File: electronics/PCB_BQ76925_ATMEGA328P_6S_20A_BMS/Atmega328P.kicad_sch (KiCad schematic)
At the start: 14 parts, among them J5 Conn_01x04, J6 Conn_02x03_Counter_Clockwise, U2 ATmega328P-A, U3 AMS1117-5.0, Y1 16Mhz

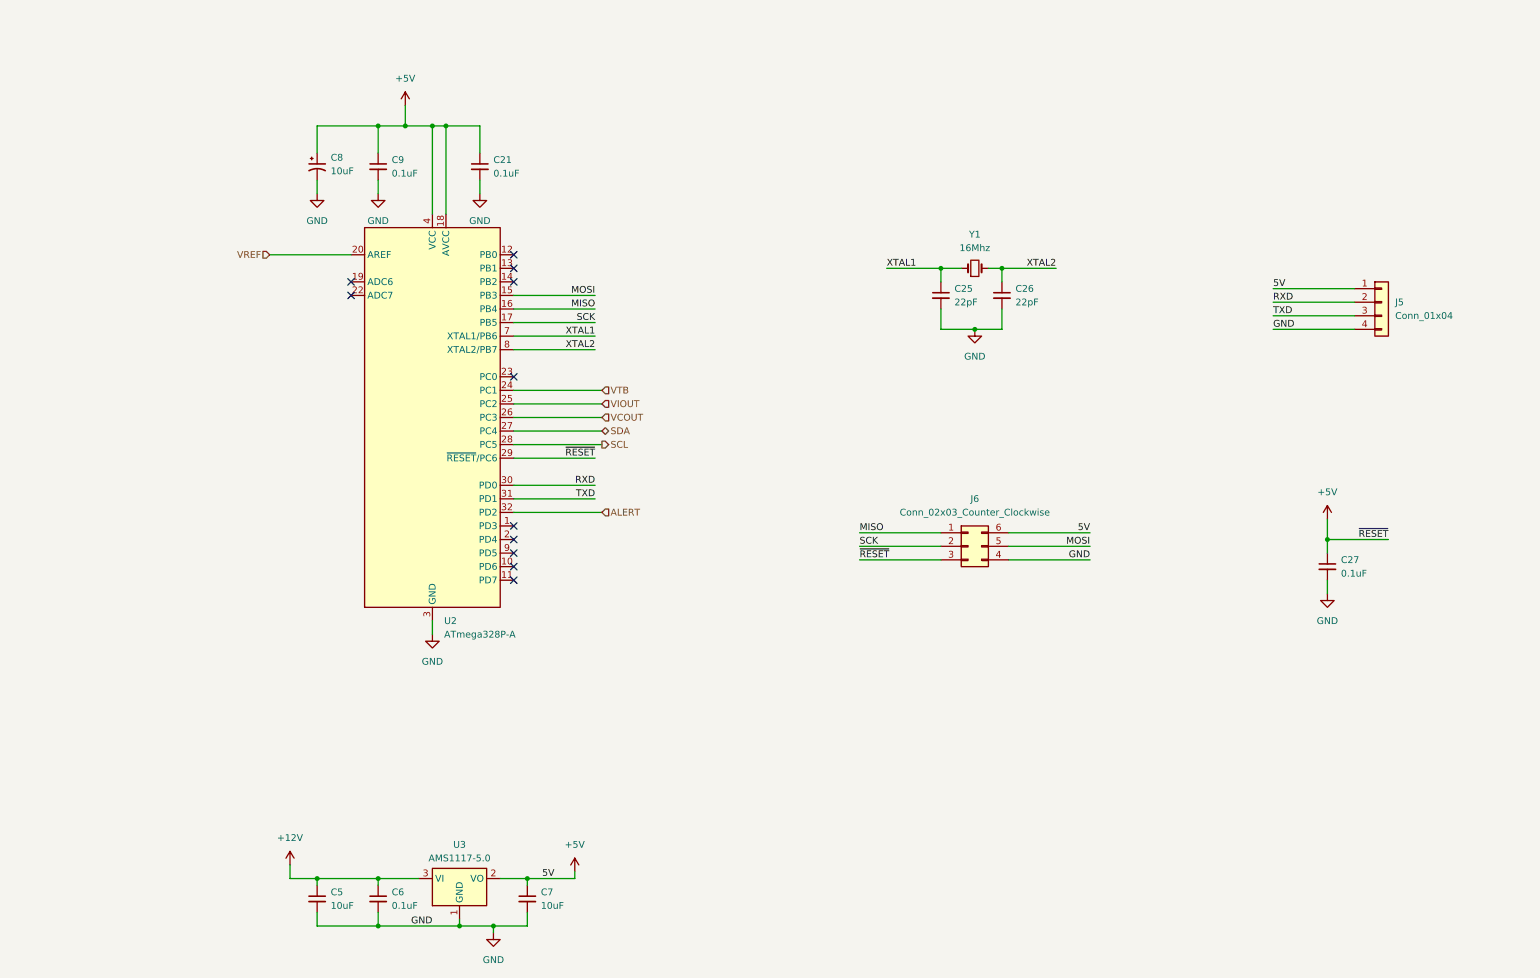
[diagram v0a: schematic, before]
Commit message: schematic completed component need to be finalised
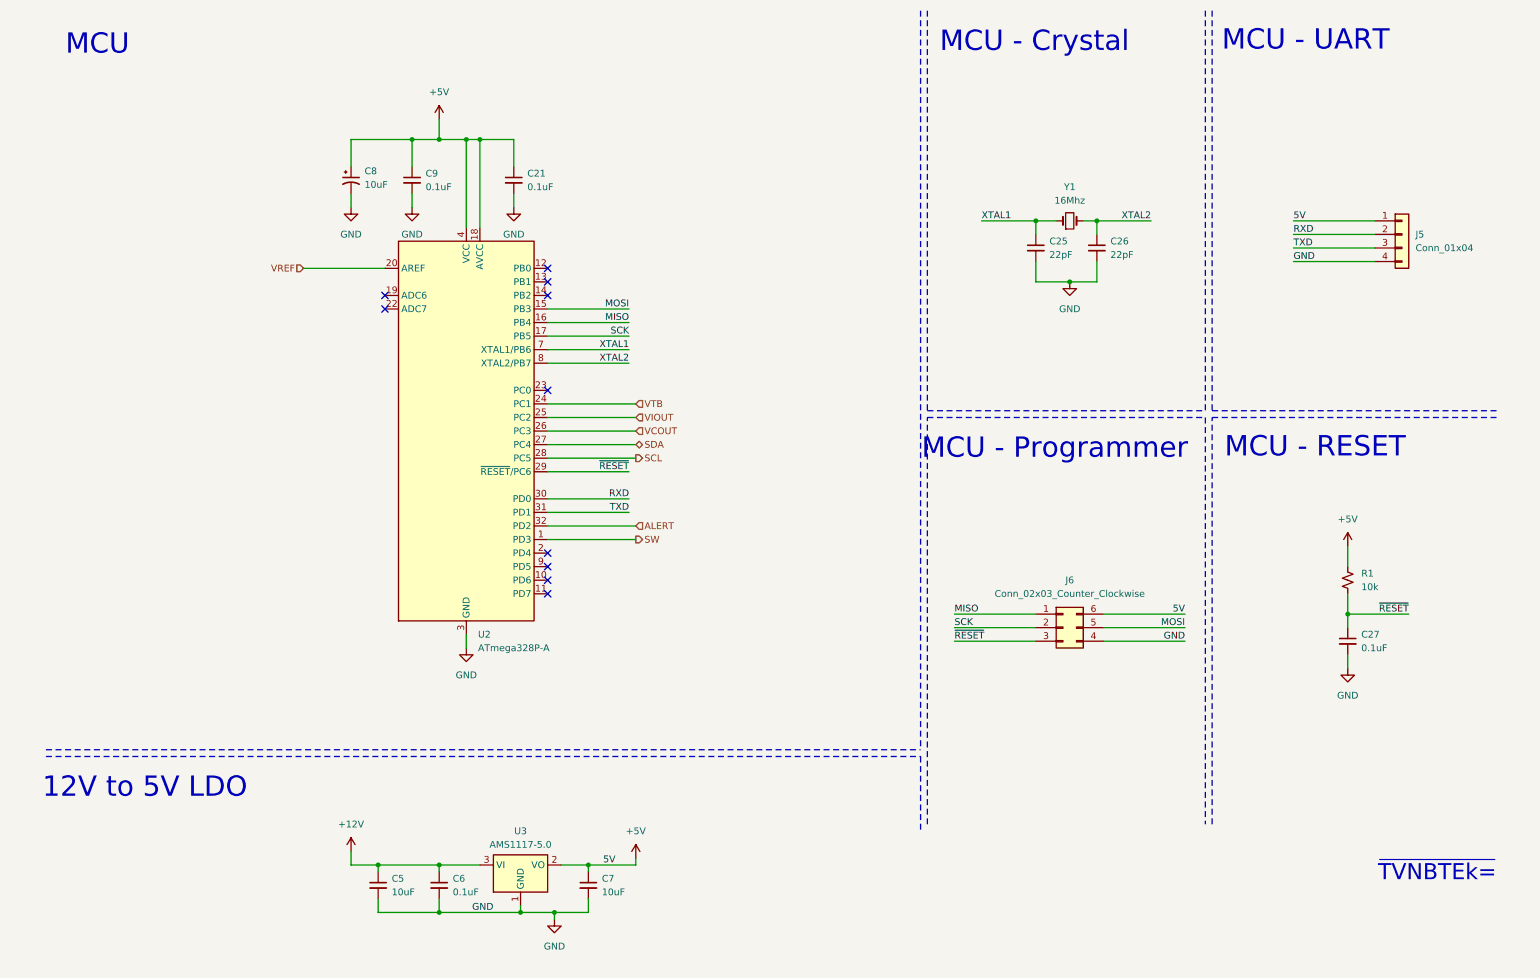
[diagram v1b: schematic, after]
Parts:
- added R1: 10k, symbol BQ76925_ATMEGA328P_6S_20A_BMS:R_Small_US
- J5: symbol Connector_Generic:Conn_01x04 -> BQ76925_ATMEGA328P_6S_20A_BMS:Conn_01x04
- J6: symbol Connector_Generic:Conn_02x03_Counter_Clockwise -> BQ76925_ATMEGA328P_6S_20A_BMS:Conn_02x03_Counter_Clockwise
- Y1: symbol Device:Crystal_Small -> BQ76925_ATMEGA328P_6S_20A_BMS:Crystal_Small
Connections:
- net +5V: now also R1.2; no longer C27.1, J6.3 (Pin_3), U2.29 (~{RESET}/PC6)
- net SW: now reaches U2.1 (PD3)
- new net ~{RESET}: C27.1, J6.3 (Pin_3), R1.1, U2.29 (~{RESET}/PC6)
- no-connect marks 11 -> 10
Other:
- note added: "12V to 5V LDO"
- note added: "MCU"
- note added: "MCU - Crystal"
- note added: "MCU - Programmer"
- note added: "MCU - RESET"
- note added: "MCU - UART"
- note added: "~{TVNBTEk=}"
- company: (none) -> M S Ali
- title: (none) -> Raven-I Sentinel
- moved on the sheet: C21, C25, C26, C27, C5, C6, C7, C8, C9, J5, J6, U2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

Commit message: Schematic completed components calculated need to check avaialability
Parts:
- C21: renamed from C9; footprint (none) -> Capacitor_SMD:C_0603_1608Metric_Pad1.08x0.95mm_HandSolder
- C22: renamed from C21; footprint (none) -> Capacitor_SMD:C_0603_1608Metric_Pad1.08x0.95mm_HandSolder
- C25: renamed from C27; footprint (none) -> Capacitor_SMD:C_0603_1608Metric_Pad1.08x0.95mm_HandSolder
- C27: renamed from C6; footprint (none) -> Capacitor_SMD:C_0603_1608Metric_Pad1.08x0.95mm_HandSolder
- J6: value Conn_02x03_Counter_Clockwise -> Conn_02x03
- R26: renamed from R1; footprint (none) -> Resistor_SMD:R_0603_1608Metric_Pad0.98x0.95mm_HandSolder
- renumbered C8 to C20, C25 to C23, C26 to C24, C5 to C26, C7 to C28, U2 to U3, U3 to U4
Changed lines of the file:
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@@
 	(title_block
 		(title "Raven-I Sentinel")
+		(date "2024-11-23")
 		(company "M S Ali")
 	)
@@
 		(dnp no)
 		(fields_autoplaced yes)
-		(property "Reference" "#PWR01"
+		(property "Reference" "#PWR032"
 			(at 91.44 138.43 0)
 			(effects
@@
 			(project "BQ76925_ATMEGA328P_6S_20A_BMS"
 				(path "/624a087f-322b-4a70-8c29-0e4f8f018e16/e88de734-726e-4991-811a-b88126c63525"
-					(reference "#PWR01")
+					(reference "#PWR032")
 					(unit 1)
 				)
@@
 		(dnp no)
 		(fields_autoplaced yes)
-		(property "Reference" "C27"
+		(property "Reference" "C25"
 			(at 259.08 129.5462 0)
 			(effects
@@
 			)
 		)
-		(property "Footprint" ""
+		(property "Footprint" "Capacitor_SMD:C_0603_1608Metric_Pad1.08x0.95mm_HandSolder"
 			(at 256.54 130.81 0)
 			(effects
@@
 			(project "BQ76925_ATMEGA328P_6S_20A_BMS"
 				(path "/624a087f-322b-4a70-8c29-0e4f8f018e16/e88de734-726e-4991-811a-b88126c63525"
-					(reference "C27")
+					(reference "C25")
 					(unit 1)
 				)
@@
 		(dnp no)
 		(fields_autoplaced yes)
-		(property "Reference" "#PWR029"
+		(property "Reference" "#PWR033"
 			(at 256.54 142.24 0)
 			(effects
@@
 			(project "BQ76925_ATMEGA328P_6S_20A_BMS"
 				(path "/624a087f-322b-4a70-8c29-0e4f8f018e16/e88de734-726e-4991-811a-b88126c63525"
-					(reference "#PWR029")
+					(reference "#PWR033")
 					(unit 1)
 				)
@@
 		(dnp no)
 		(fields_autoplaced yes)
-		(property "Reference" "C25"
+		(property "Reference" "C23"
 			(at 200.66 55.8862 0)
 			(effects
@@
 			(project "BQ76925_ATMEGA328P_6S_20A_BMS"
 				(path "/624a087f-322b-4a70-8c29-0e4f8f018e16/e88de734-726e-4991-811a-b88126c63525"
-					(reference "C25")
+					(reference "C23")
 					(unit 1)
 				)
@@
 		(dnp no)
 		(fields_autoplaced yes)
-		(property "Reference" "C6"
+		(property "Reference" "C27"
 			(at 88.9 175.2662 0)
 			(effects
@@
 			)
 		)
-		(property "Footprint" ""
+		(property "Footprint" "Capacitor_SMD:C_0603_1608Metric_Pad1.08x0.95mm_HandSolder"
 			(at 86.36 176.53 0)
 			(effects
@@
 			(project "BQ76925_ATMEGA328P_6S_20A_BMS"
 				(path "/624a087f-322b-4a70-8c29-0e4f8f018e16/e88de734-726e-4991-811a-b88126c63525"
-					(reference "C6")
+					(reference "C27")
 					(unit 1)
 				)
@@
 		(dnp no)
 		(fields_autoplaced yes)
-		(property "Reference" "R1"
+		(property "Reference" "R26"
 			(at 259.08 118.1099 0)
 			(effects
@@
 			)
 		)
-		(property "Footprint" ""
+		(property "Footprint" "Resistor_SMD:R_0603_1608Metric_Pad0.98x0.95mm_HandSolder"
 			(at 256.54 119.38 0)
 			(effects
@@
 			(project "BQ76925_ATMEGA328P_6S_20A_BMS"
 				(path "/624a087f-322b-4a70-8c29-0e4f8f018e16/e88de734-726e-4991-811a-b88126c63525"
-					(reference "R1")
+					(reference "R26")
 					(unit 1)
 				)
@@
 		(dnp no)
 		(fields_autoplaced yes)
-		(property "Reference" "#PWR023"
+		(property "Reference" "#PWR027"
 			(at 69.85 55.88 0)
 			(effects
@@
 			(project "BQ76925_ATMEGA328P_6S_20A_BMS"
 				(path "/624a087f-322b-4a70-8c29-0e4f8f018e16/e88de734-726e-4991-811a-b88126c63525"
-					(reference "#PWR023")
+					(reference "#PWR027")
 					(unit 1)
 				)
@@
 		(dnp no)
 		(fields_autoplaced yes)
-		(property "Reference" "#PWR06"
+		(property "Reference" "#PWR035"
 			(at 123.19 175.26 0)
 			(effects
@@
 			(project "BQ76925_ATMEGA328P_6S_20A_BMS"
 				(path "/624a087f-322b-4a70-8c29-0e4f8f018e16/e88de734-726e-4991-811a-b88126c63525"
-					(reference "#PWR06")
+					(reference "#PWR035")
 					(unit 1)
 				)
@@
 		(dnp no)
 		(fields_autoplaced yes)
-		(property "Reference" "U2"
+		(property "Reference" "U3"
 			(at 93.6341 129.54 0)
 			(effects
@@
 			(project "BQ76925_ATMEGA328P_6S_20A_BMS"
 				(path "/624a087f-322b-4a70-8c29-0e4f8f018e16/e88de734-726e-4991-811a-b88126c63525"
-					(reference "U2")
+					(reference "U3")
 					(unit 1)
 				)
@@
 		(dnp no)
 		(fields_autoplaced yes)
-		(property "Reference" "#PWR028"
+		(property "Reference" "#PWR031"
 			(at 256.54 116.84 0)
 			(effects
@@
 			(project "BQ76925_ATMEGA328P_6S_20A_BMS"
 				(path "/624a087f-322b-4a70-8c29-0e4f8f018e16/e88de734-726e-4991-811a-b88126c63525"
-					(reference "#PWR028")
+					(reference "#PWR031")
 					(unit 1)
 				)
@@
 		(dnp no)
 		(fields_autoplaced yes)
-		(property "Reference" "#PWR03"
+		(property "Reference" "#PWR036"
 			(at 107.95 189.23 0)
 			(effects
@@
 			(project "BQ76925_ATMEGA328P_6S_20A_BMS"
 				(path "/624a087f-322b-4a70-8c29-0e4f8f018e16/e88de734-726e-4991-811a-b88126c63525"
-					(reference "#PWR03")
+					(reference "#PWR036")
 					(unit 1)
 				)
@@
 		(dnp no)
 		(fields_autoplaced yes)
-		(property "Reference" "C5"
+		(property "Reference" "C26"
 			(at 77.47 175.2662 0)
 			(effects
@@
 			(project "BQ76925_ATMEGA328P_6S_20A_BMS"
 				(path "/624a087f-322b-4a70-8c29-0e4f8f018e16/e88de734-726e-4991-811a-b88126c63525"
-					(reference "C5")
+					(reference "C26")
 					(unit 1)
 				)
@@
 		(dnp no)
 		(fields_autoplaced yes)
-		(property "Reference" "C9"
+		(property "Reference" "C21"
 			(at 83.82 43.1862 0)
 			(effects
@@
 			)
 		)
-		(property "Footprint" ""
+		(property "Footprint" "Capacitor_SMD:C_0603_1608Metric_Pad1.08x0.95mm_HandSolder"
 			(at 81.28 44.45 0)
 			(effects
@@
 			(project "BQ76925_ATMEGA328P_6S_20A_BMS"
 				(path "/624a087f-322b-4a70-8c29-0e4f8f018e16/e88de734-726e-4991-811a-b88126c63525"
-					(reference "C9")
+					(reference "C21")
 					(unit 1)
 				)
@@
 		(dnp no)
 		(fields_autoplaced yes)
-		(property "Reference" "C8"
+		(property "Reference" "C20"
 			(at 72.39 42.7481 0)
 			(effects
@@
 			(project "BQ76925_ATMEGA328P_6S_20A_BMS"
 				(path "/624a087f-322b-4a70-8c29-0e4f8f018e16/e88de734-726e-4991-811a-b88126c63525"
-					(reference "C8")
+					(reference "C20")
 					(unit 1)
 				)
@@
 		(dnp no)
 		(fields_autoplaced yes)
-		(property "Reference" "#PWR04"
+		(property "Reference" "#PWR034"
 			(at 69.85 173.99 0)
 			(effects
@@
 			(project "BQ76925_ATMEGA328P_6S_20A_BMS"
 				(path "/624a087f-322b-4a70-8c29-0e4f8f018e16/e88de734-726e-4991-811a-b88126c63525"
-					(reference "#PWR04")
+					(reference "#PWR034")
 					(unit 1)
 				)
@@
 		(dnp no)
 		(fields_autoplaced yes)
-		(property "Reference" "C7"
+		(property "Reference" "C28"
 			(at 116.84 175.2662 0)
 			(effects
@@
 			(project "BQ76925_ATMEGA328P_6S_20A_BMS"
 				(path "/624a087f-322b-4a70-8c29-0e4f8f018e16/e88de734-726e-4991-811a-b88126c63525"
-					(reference "C7")
+					(reference "C28")
 					(unit 1)
 				)
@@
 		(dnp no)
 		(fields_autoplaced yes)
-		(property "Reference" "#PWR024"
+		(property "Reference" "#PWR026"
 			(at 86.36 36.83 0)
 			(effects
@@
 			(project "BQ76925_ATMEGA328P_6S_20A_BMS"
 				(path "/624a087f-322b-4a70-8c29-0e4f8f018e16/e88de734-726e-4991-811a-b88126c63525"
-					(reference "#PWR024")
+					(reference "#PWR026")
 					(unit 1)
 				)
@@
 		(dnp no)
 		(fields_autoplaced yes)
-		(property "Reference" "#PWR027"
+		(property "Reference" "#PWR030"
 			(at 204.47 69.85 0)
 			(effects
@@
 			(project "BQ76925_ATMEGA328P_6S_20A_BMS"
 				(path "/624a087f-322b-4a70-8c29-0e4f8f018e16/e88de734-726e-4991-811a-b88126c63525"
-					(reference "#PWR027")
+					(reference "#PWR030")
 					(unit 1)
 				)
@@
 		(dnp no)
 		(fields_autoplaced yes)
-		(property "Reference" "#PWR026"
+		(property "Reference" "#PWR029"
 			(at 100.33 55.88 0)
 			(effects
@@
 			(project "BQ76925_ATMEGA328P_6S_20A_BMS"
 				(path "/624a087f-322b-4a70-8c29-0e4f8f018e16/e88de734-726e-4991-811a-b88126c63525"
-					(reference "#PWR026")
+					(reference "#PWR029")
 					(unit 1)
 				)
@@
 		(dnp no)
 		(fields_autoplaced yes)
-		(property "Reference" "U3"
+		(property "Reference" "U4"
 			(at 101.6 166.37 0)
 			(effects
@@
 			(project "BQ76925_ATMEGA328P_6S_20A_BMS"
 				(path "/624a087f-322b-4a70-8c29-0e4f8f018e16/e88de734-726e-4991-811a-b88126c63525"
-					(reference "U3")
+					(reference "U4")
 					(unit 1)
 				)
@@
 			)
 		)
-		(property "Value" "Conn_02x03_Counter_Clockwise"
+		(property "Value" "Conn_02x03"
 			(at 204.47 121.92 0)
 			(effects
@@
 		(dnp no)
 		(fields_autoplaced yes)
-		(property "Reference" "C21"
+		(property "Reference" "C22"
 			(at 102.87 43.1862 0)
 			(effects
@@
 			)
 		)
-		(property "Footprint" ""
+		(property "Footprint" "Capacitor_SMD:C_0603_1608Metric_Pad1.08x0.95mm_HandSolder"
 			(at 100.33 44.45 0)
 			(effects
@@
 			(project "BQ76925_ATMEGA328P_6S_20A_BMS"
 				(path "/624a087f-322b-4a70-8c29-0e4f8f018e16/e88de734-726e-4991-811a-b88126c63525"
-					(reference "C21")
+					(reference "C22")
 					(unit 1)
 				)
@@
 		(dnp no)
 		(fields_autoplaced yes)
-		(property "Reference" "#PWR025"
+		(property "Reference" "#PWR028"
 			(at 81.28 55.88 0)
 			(effects
@@
 			(project "BQ76925_ATMEGA328P_6S_20A_BMS"
 				(path "/624a087f-322b-4a70-8c29-0e4f8f018e16/e88de734-726e-4991-811a-b88126c63525"
-					(reference "#PWR025")
+					(reference "#PWR028")
 					(unit 1)
 				)
@@
 		(dnp no)
 		(fields_autoplaced yes)
-		(property "Reference" "C26"
+		(property "Reference" "C24"
 			(at 212.09 55.8862 0)
 			(effects
@@
 			(project "BQ76925_ATMEGA328P_6S_20A_BMS"
 				(path "/624a087f-322b-4a70-8c29-0e4f8f018e16/e88de734-726e-4991-811a-b88126c63525"
-					(reference "C26")
+					(reference "C24")
 					(unit 1)
 				)

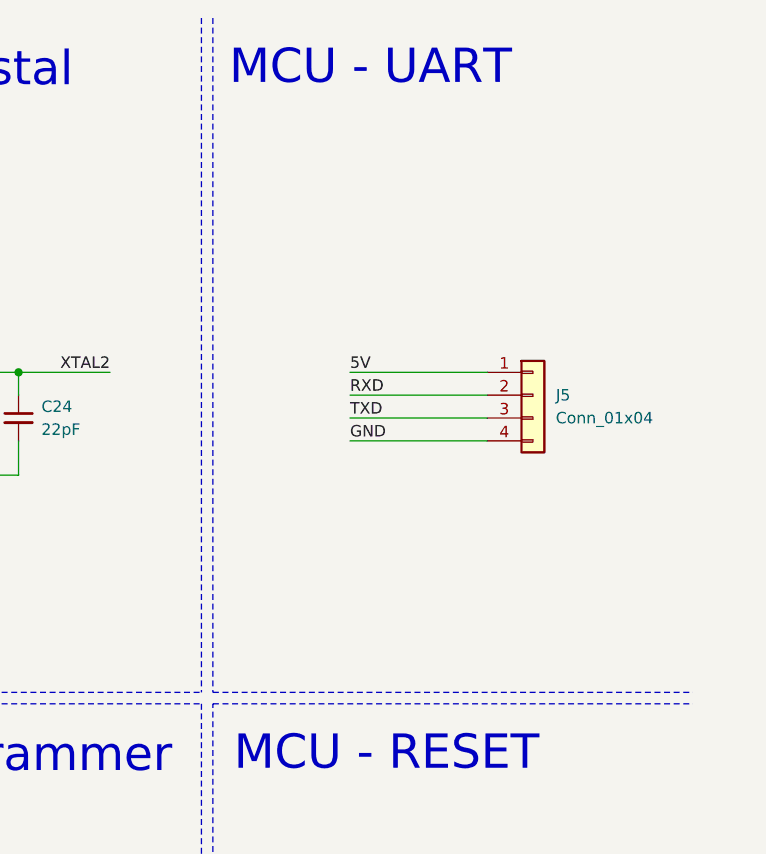
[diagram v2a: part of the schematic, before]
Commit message: added power led and mcu test led in schematic
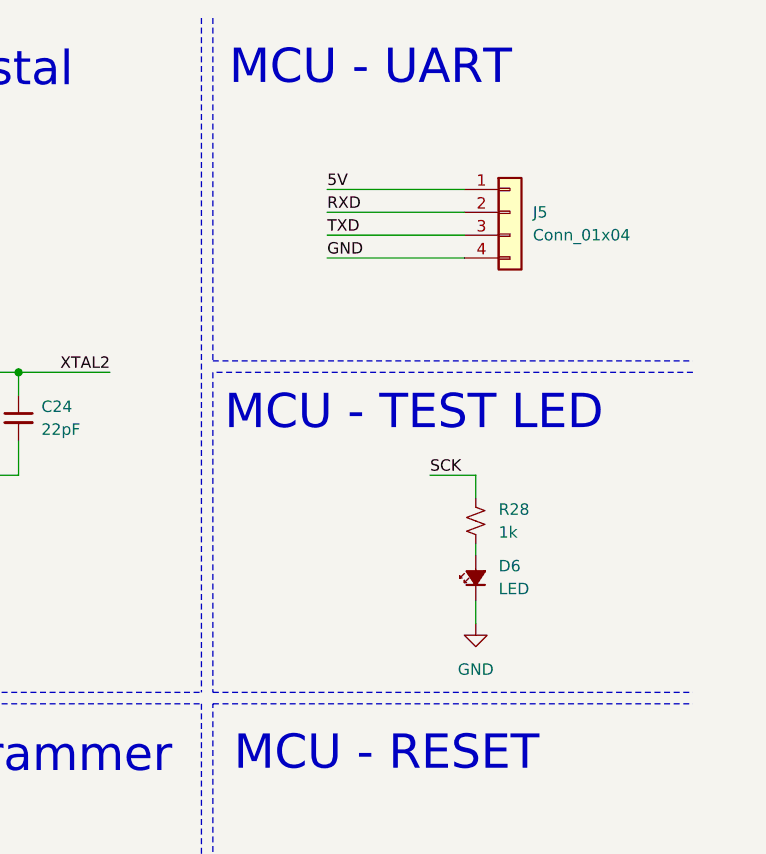
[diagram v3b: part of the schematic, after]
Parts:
- added D6: LED, symbol Device:LED_Small_Filled
- added R28: 1k, Resistor_SMD:R_0603_1608Metric_Pad0.98x0.95mm_HandSolder, symbol BQ76925_ATMEGA328P_6S_20A_BMS:R_Small_US
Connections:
- net GND: now also D6.1 (K)
- net SCK: now also R28.1
- new net: D6.2 (A), R28.2
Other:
- note added: "MCU - TEST LED"
- moved on the sheet: J5
